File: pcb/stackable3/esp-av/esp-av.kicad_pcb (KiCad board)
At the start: 2 copper layers, 100 x 66 mm, 129 parts, among them J0 DC-005, J1 USB_C_Receptacle_USB2.0_16P, J10 JST SH, J11 STEMMA-Signal, J12 Qwiic, J13 Qwiic, J14 Pin socket, J15 Pin Socket, J16 Pin socket, J2 PJ-327U, J3 PJ-327U, J4 PJ-327U, J5 PJ-327U, J6 PJ-327U, J7 PJ-327U, J8 PJ-327U, J9 PJ-327U, Q1 PDNM6ET20V05, Q10 DMP1045U, Q11 DMP1045U, Q12 DMP1045U, Q13 DMP1045U, Q2 DMG6968U, Q3 DMP1045U, Q4 DMP1045U, Q5 DMP1045U, Q6 DMP1045U, Q7 PDNM6ET20V05, Q8 PDNM6ET20V05, Q9 PDNM6ET20V05, SW1 Reset, SW2 Boot, U1 USBLC6-2P6, U10 SN74LVC1T45Z6, U11 SN74LVC1T45Z6, U12 74HC595, U13 74HC595, U2 ME6211C33M5, U3 TPS563201, U4 NC7WZ14P6X, U5 NC7WZ14P6X, U6 SN74LVC1G157DC, U7 SN74LVC1G157DC, U8 SN74LVC1G157DC, U9 SN74LVC1G157DC

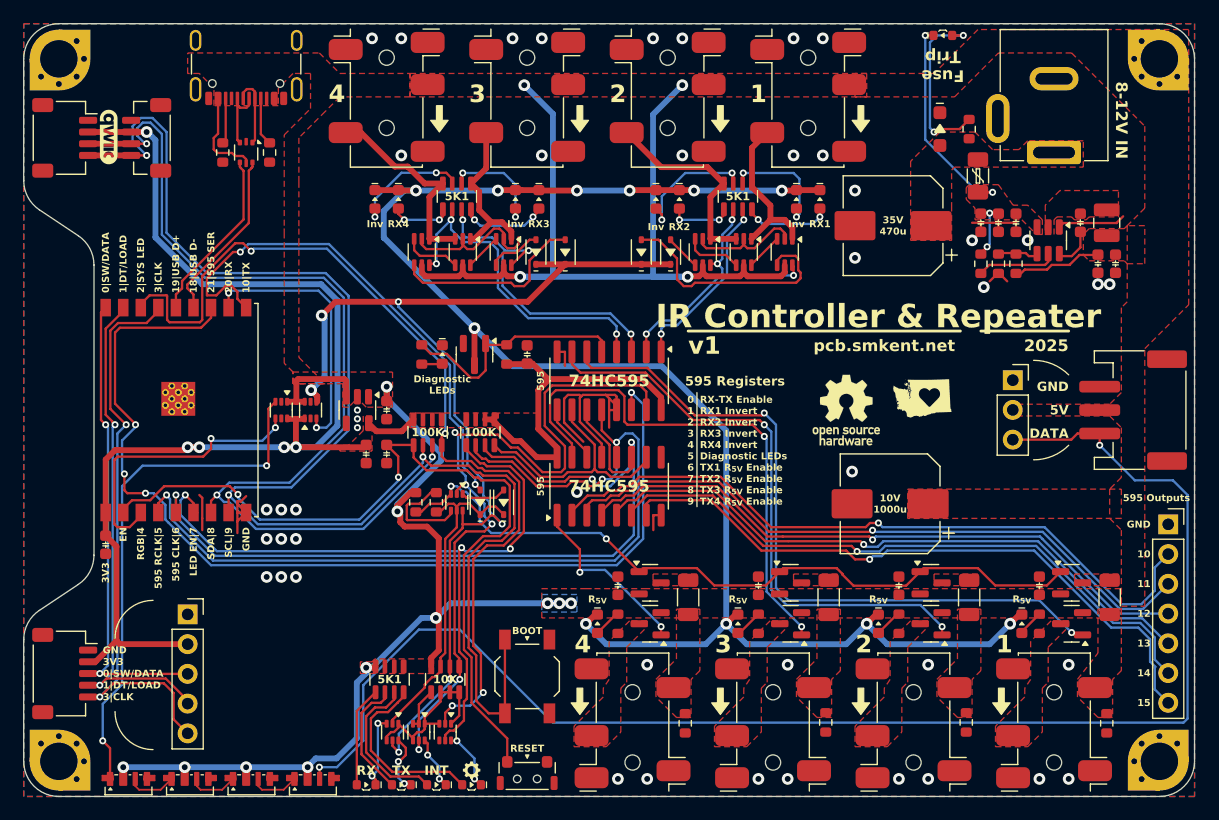
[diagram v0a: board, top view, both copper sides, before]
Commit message: Tweak power traces on stackable3/esp-av
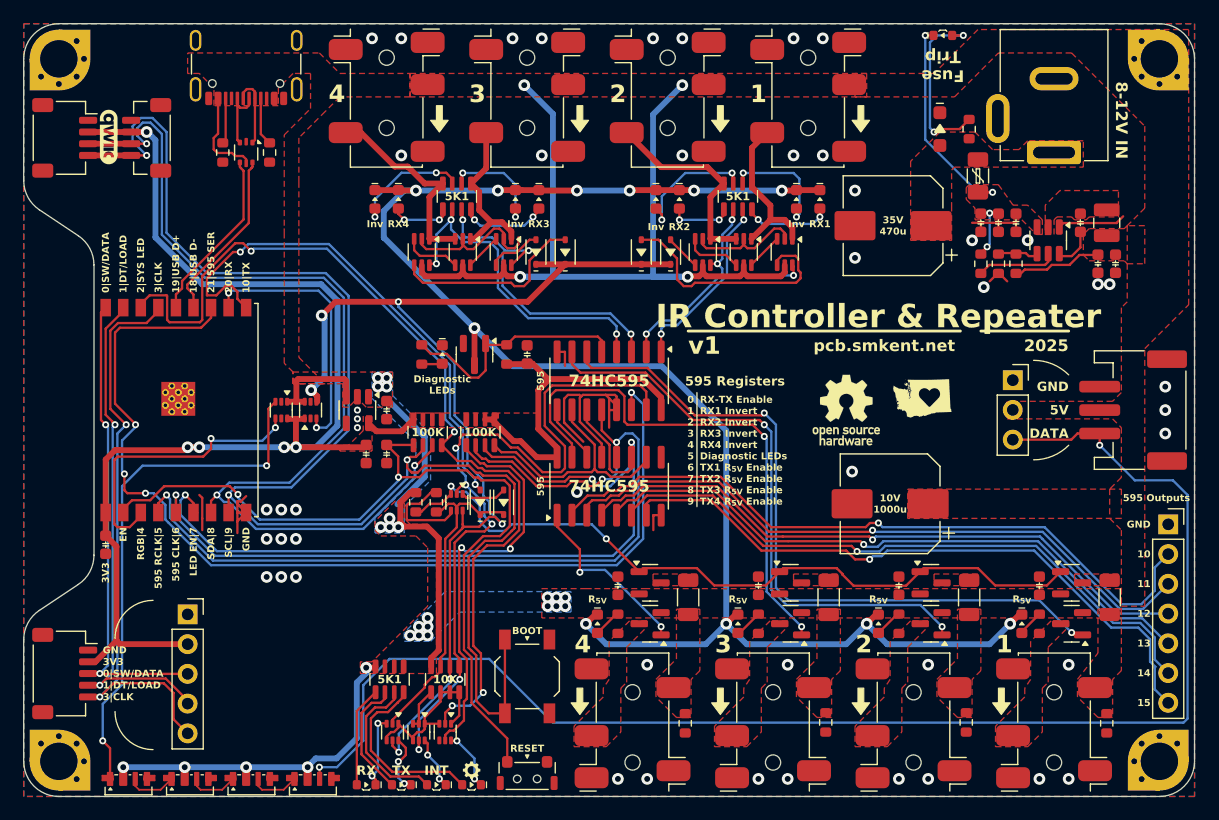
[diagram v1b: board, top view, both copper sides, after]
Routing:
- net +5V: track 187.4 -> 163.1 mm, vias 15 -> 29
- net IO9/SCL: track 124.2 -> 126.6 mm
- net PIXEL_DOUT: track 123.2 -> 121.2 mm
- net RX_TX_EN: track 63.1 -> 62.4 mm
- net GND: vias 46 -> 49

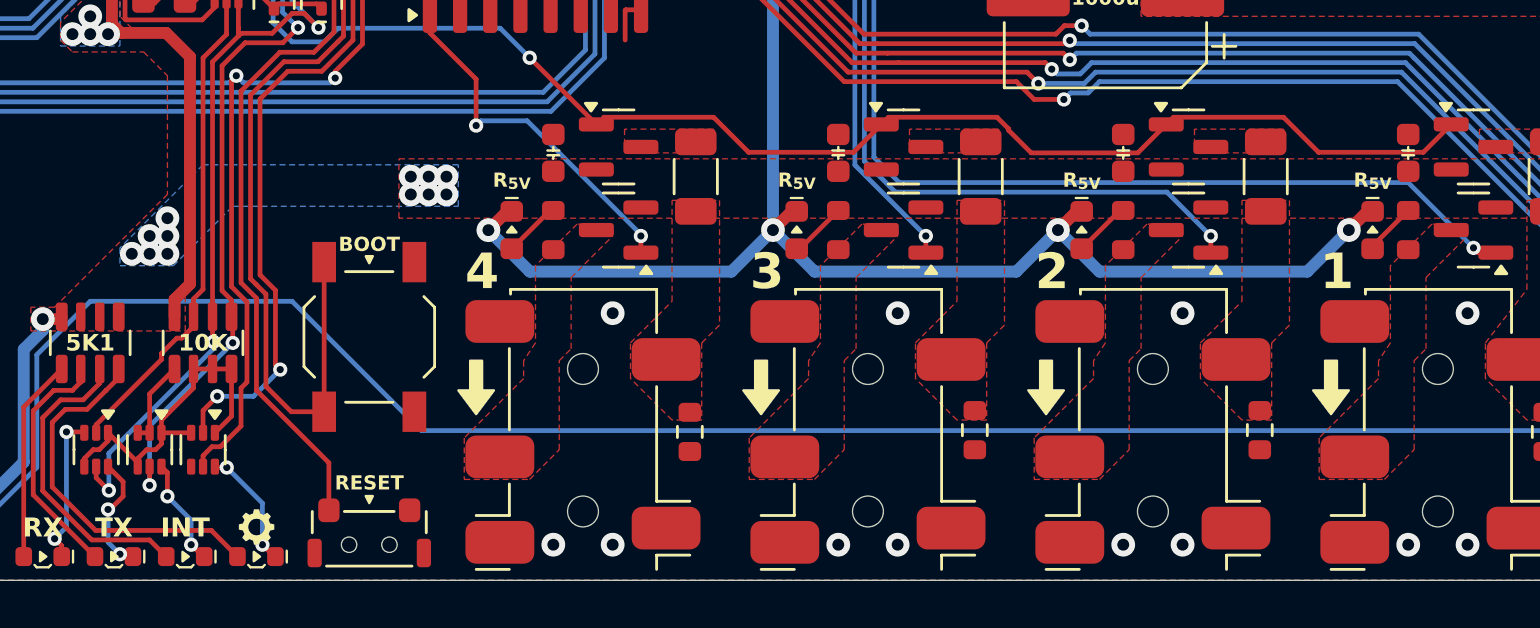
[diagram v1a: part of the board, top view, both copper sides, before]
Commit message: Tweak silkscreen
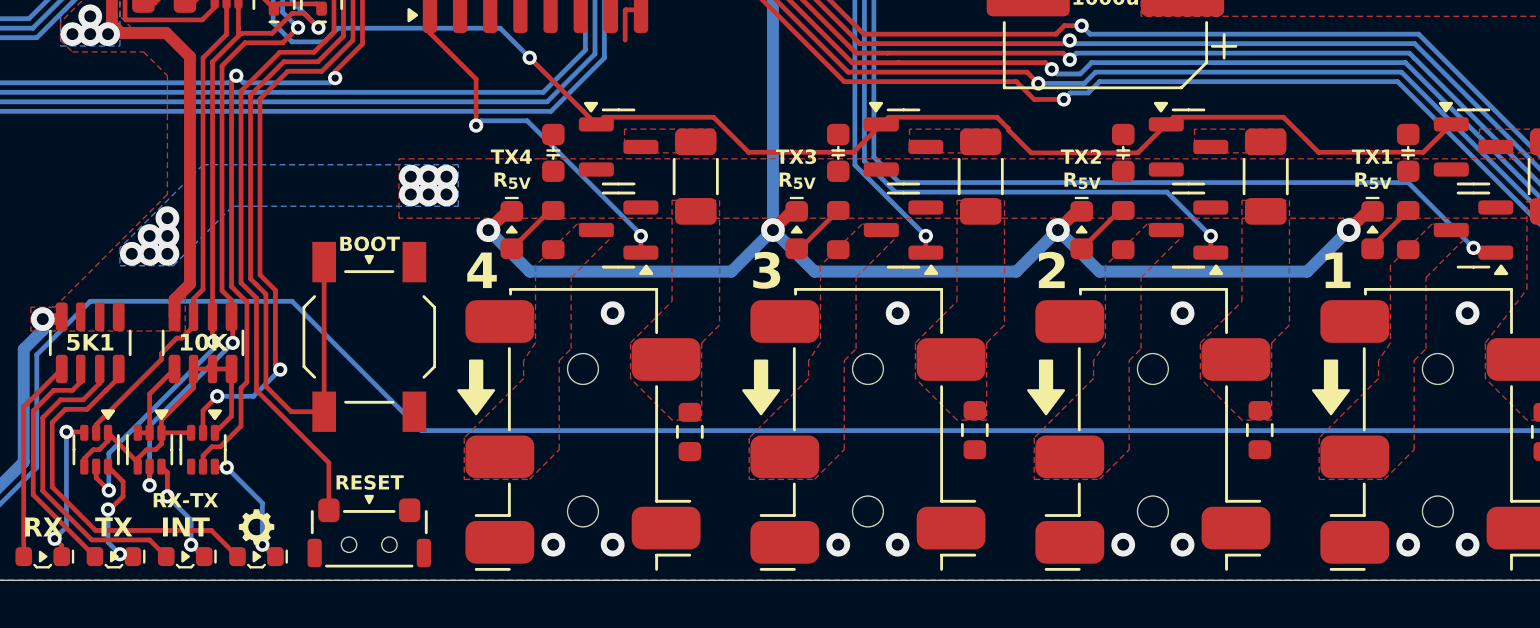
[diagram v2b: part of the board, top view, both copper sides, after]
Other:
- board text added: "RX-TX"
- board text added: "TX1 R_{5V}"
- board text added: "TX2 R_{5V}"
- board text added: "TX3 R_{5V}"
- board text added: "TX4 R_{5V}"
- board text removed: "R_{5V}"
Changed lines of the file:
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@@
 		)
 	)
-	(gr_text "R_{5V}"
+	(gr_text "TX3\nR_{5V}"
 		(at 183 103.5 0)
 		(layer "F.SilkS")
@@
 		)
 	)
-	(gr_text "R_{5V}"
+	(gr_text "TX1\nR_{5V}"
 		(at 207.25 103.5 0)
 		(layer "F.SilkS")
@@
 		)
 	)
-	(gr_text "R_{5V}"
+	(gr_text "TX4\nR_{5V}"
 		(at 171 103.5 0)
 		(layer "F.SilkS")
@@
 		)
 	)
-	(gr_text "R_{5V}"
+	(gr_text "TX2\nR_{5V}"
 		(at 195 103.5 0)
 		(layer "F.SilkS")
@@
 		)
 	)
+	(gr_text "RX-TX"
+		(at 157.25 117 0)
+		(layer "F.SilkS")
+		(effects
+			(font
+				(size 0.6 0.6)
+				(thickness 0.12)
+				(bold yes)
+			)
+			(justify bottom)
+		)
+	)

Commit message: Change repeater enable silkscreen text
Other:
- board text added: "IR Repeater Enable RX1 Invert RX2 Invert RX3 Invert RX4 Invert Diagnostic LEDs TX1 R_{5V} Enable TX2 R_{5V} Enable TX3 R_{5V} Enable TX4 R_{5V} Enable"
- board text added: "No Repeat"
- board text removed: "INT"
- board text removed: "RX-TX"
- board text removed: "RX-TX Enable RX1 Invert RX2 Invert RX3 Invert RX4 Invert Diagnostic LEDs TX1 R_{5V} Enable TX2 R_{5V} Enable TX3 R_{5V} Enable TX4 R_{5V} Enable"
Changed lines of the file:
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@@
 		)
 	)
-	(gr_text "RX-TX Enable\nRX1 Invert\nRX2 Invert\nRX3 Invert\nRX4 Invert\nDiagnostic LEDs\nTX1 R_{5V} Enable\nTX2 R_{5V} Enable\nTX3 R_{5V} Enable\nTX4 R_{5V} Enable"
+	(gr_text "IR Repeater Enable\nRX1 Invert\nRX2 Invert\nRX3 Invert\nRX4 Invert\nDiagnostic LEDs\nTX1 R_{5V} Enable\nTX2 R_{5V} Enable\nTX3 R_{5V} Enable\nTX4 R_{5V} Enable"
 		(at 179.75 85.75 0)
 		(layer "F.SilkS")
@@
 				)
 			)
-		)
-	)
-	(gr_text "INT"
-		(at 157.25 118.25 0)
-		(layer "F.SilkS")
-		(effects
-			(font
-				(size 0.8 0.8)
-				(thickness 0.16)
-				(bold yes)
-			)
-			(justify bottom)
 		)
 	)
@@
 		)
 	)
-	(gr_text "RX-TX"
-		(at 157.25 117 0)
-		(layer "F.SilkS")
-		(effects
+	(gr_text "No\nRepeat"
+		(at 157.25 118.25 0)
+		(layer "F.SilkS")
+		(effects

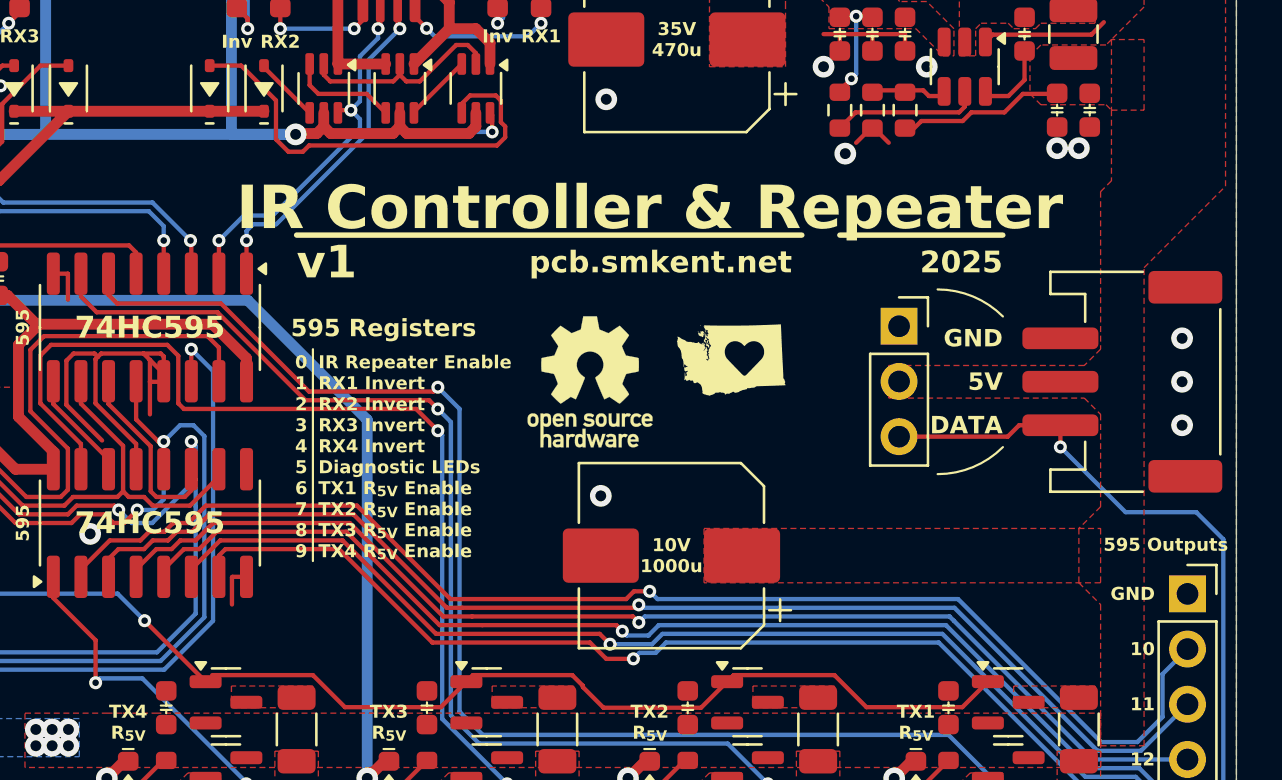
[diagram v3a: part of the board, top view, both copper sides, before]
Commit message: Add more mounting holes to stackable3/esp-av
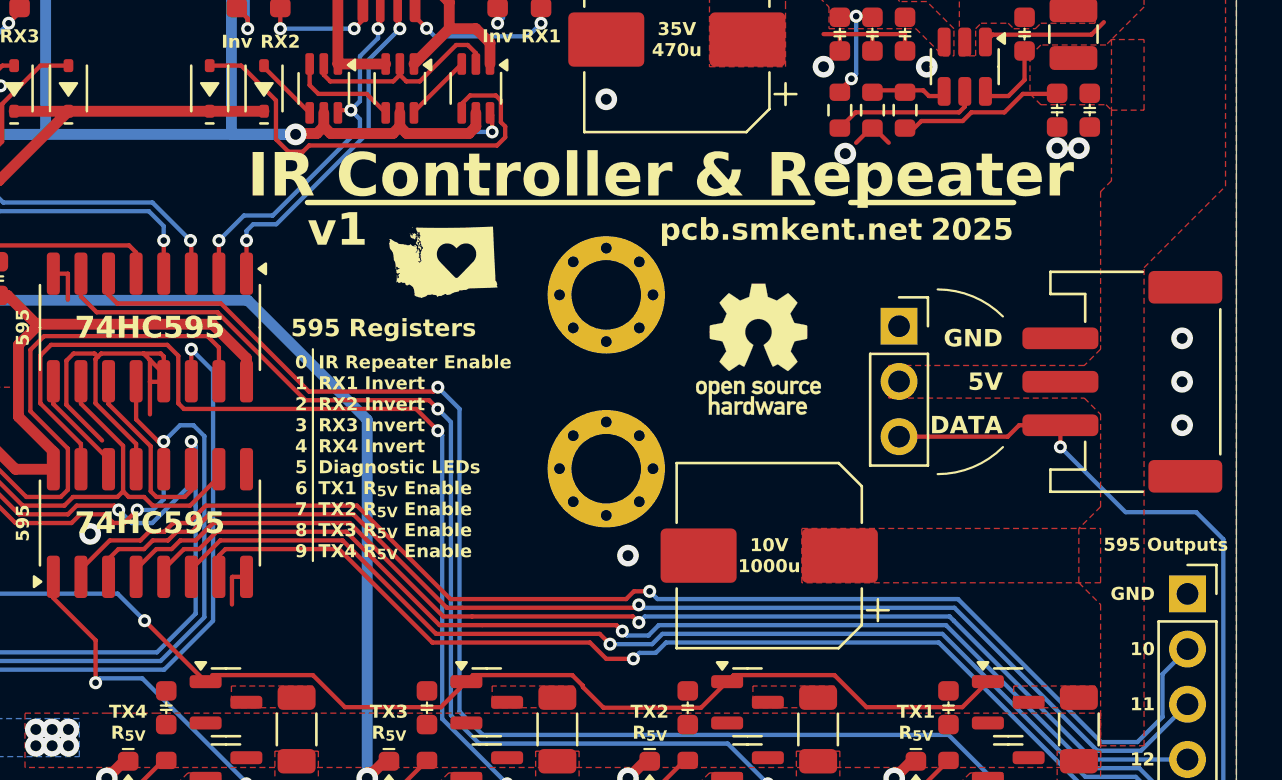
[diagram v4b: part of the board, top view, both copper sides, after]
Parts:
- added REF**: MountingHole_3.2mm_M3_5.4mm_Pad_Via, mechanical:MountingHole_3.2mm_M3_5.4mm_Pad_Via, F.Cu at (193.0, 91.0)
- added REF**: MountingHole_3.2mm_M3_5.4mm_Pad_Via, mechanical:MountingHole_3.2mm_M3_5.4mm_Pad_Via, F.Cu at (193.0, 83.0)
- moved G*** 14.0 mm to (185.5, 81.5)
- moved REF** 7.89 mm to (200.0, 85.5)
- moved C9 4.50 mm to (200.5, 95.0)

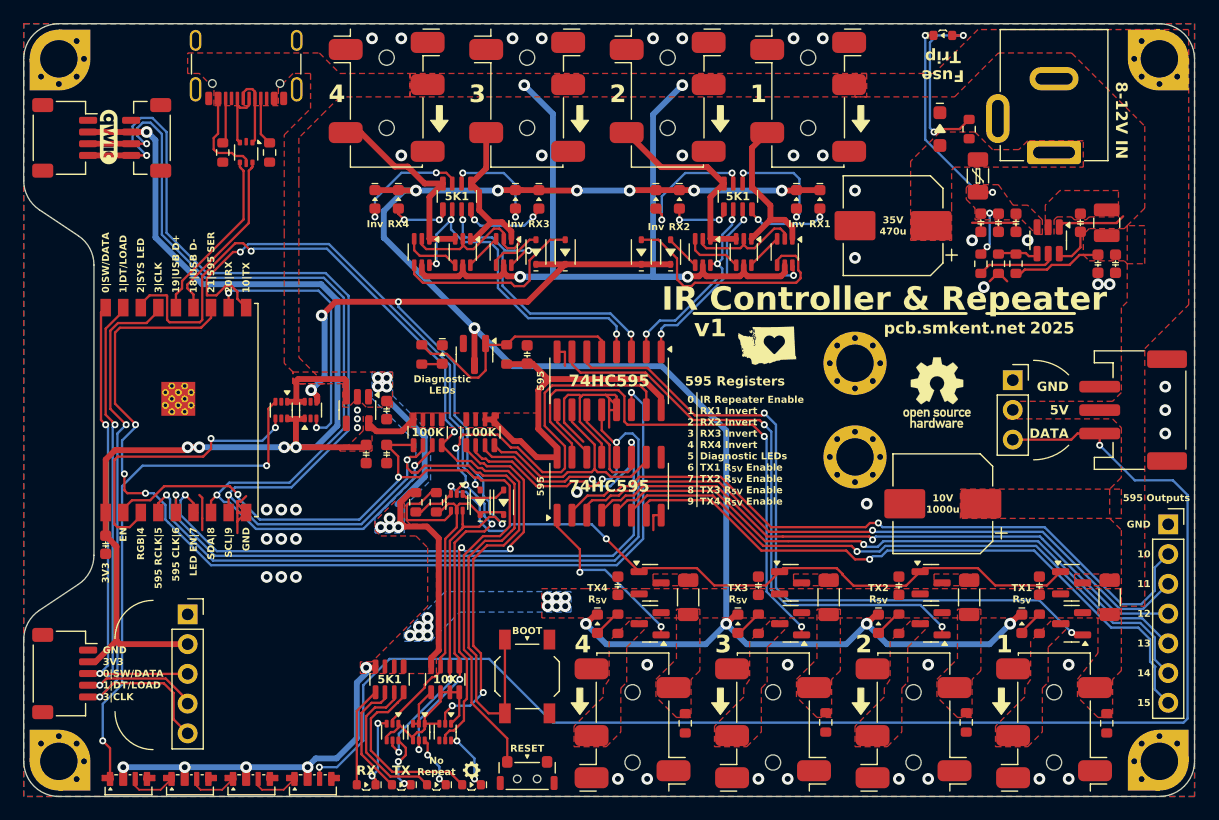
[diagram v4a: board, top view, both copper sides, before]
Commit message: Rearrange power capacitors
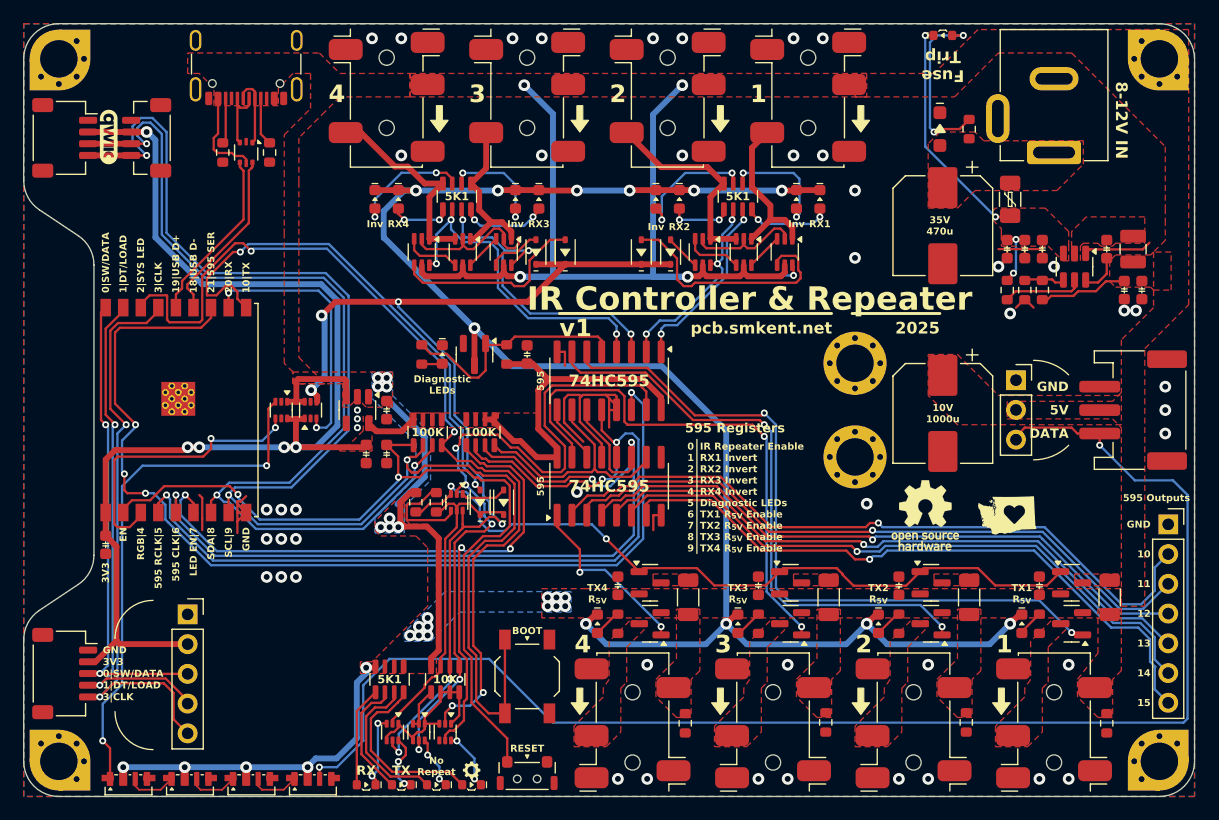
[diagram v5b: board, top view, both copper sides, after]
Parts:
- moved G*** 25.1 mm to (206.0, 96.0)
- moved REF** 10.5 mm to (199.0, 96.0)
- moved C9 7.72 mm to (200.5, 87.3), turned to -90 degrees
- moved C16 4.25 mm to (200.5, 71.2), turned to -90 degrees
- moved F1 3.40 mm to (206.2, 69.0)
- moved C10 3.18 mm to (206.0, 73.2)
- moved C11 3.18 mm to (207.5, 73.2)
- moved C12 3.18 mm to (209.0, 73.2)
- moved C13 3.18 mm to (214.5, 73.2)
- moved C14 3.18 mm to (216.0, 76.8)
- moved C15 3.18 mm to (217.5, 76.8)
- moved L1 3.18 mm to (216.8, 73.2)
- moved R3 3.18 mm to (206.0, 76.8)
- moved R8 3.18 mm to (209.0, 76.8)
- moved R9 3.18 mm to (207.5, 76.8)
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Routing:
- net +12V: track 23.0 -> 24.5 mm
